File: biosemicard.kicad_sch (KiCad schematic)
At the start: 10 parts, among them J1 Conn_01x12_Pin, J2 Conn_01x08_Pin, U2 74HC151D

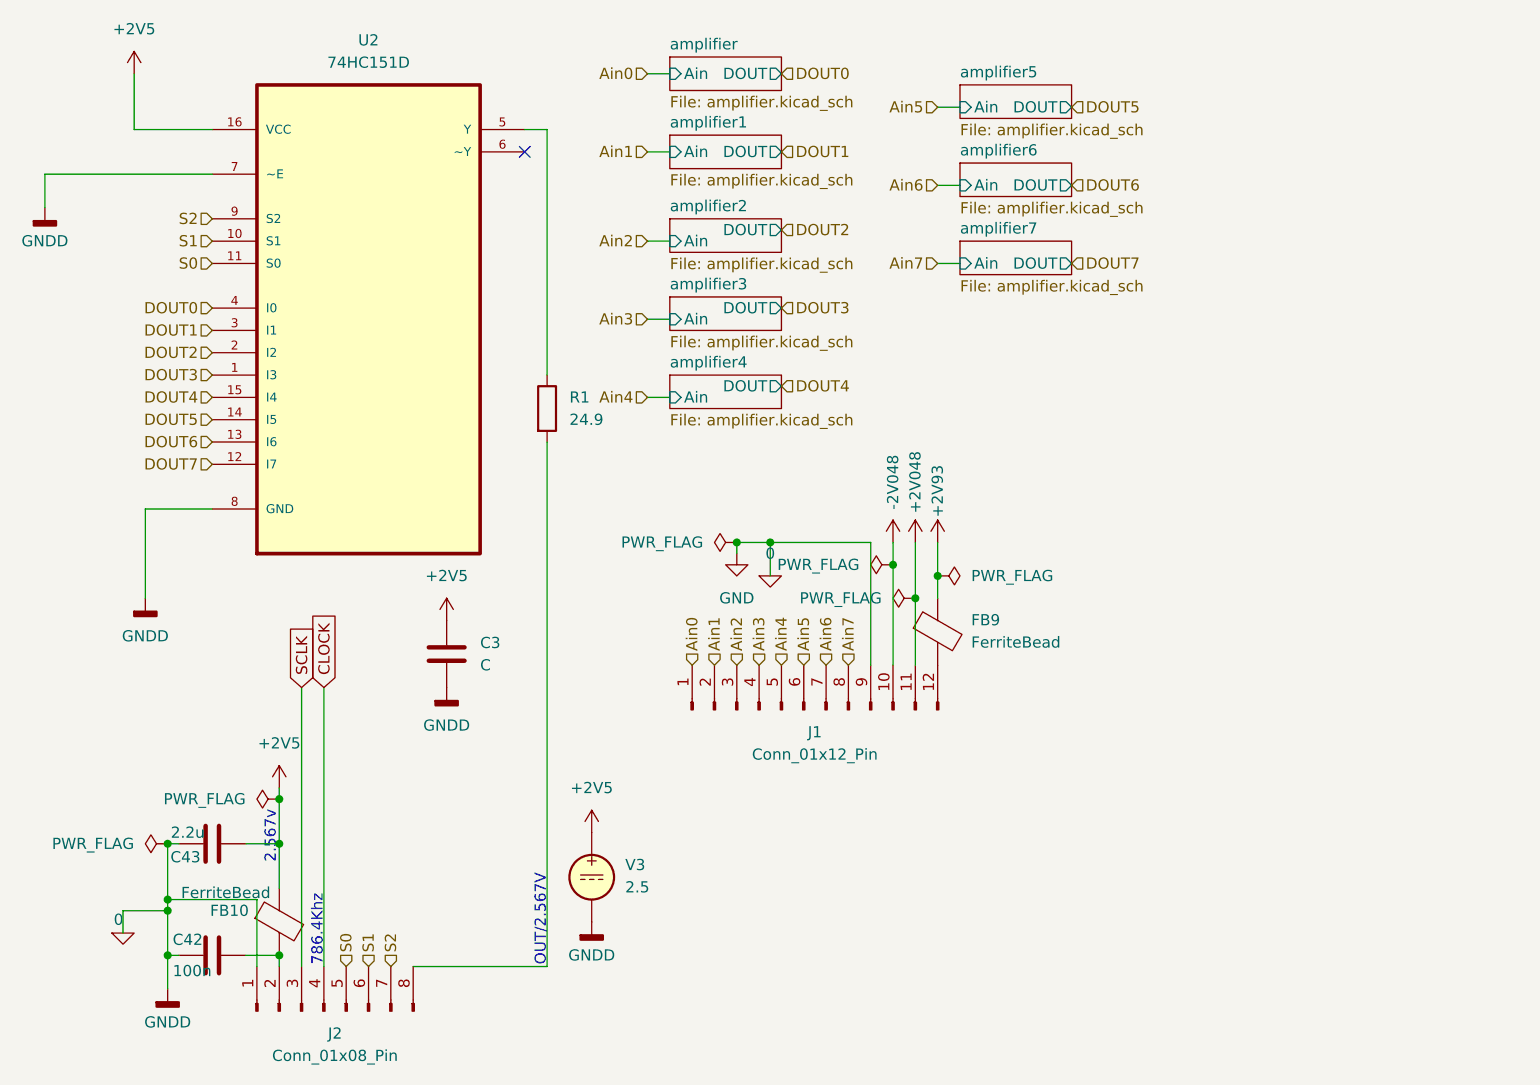
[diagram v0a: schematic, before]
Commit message: added components, updated pcb-routing
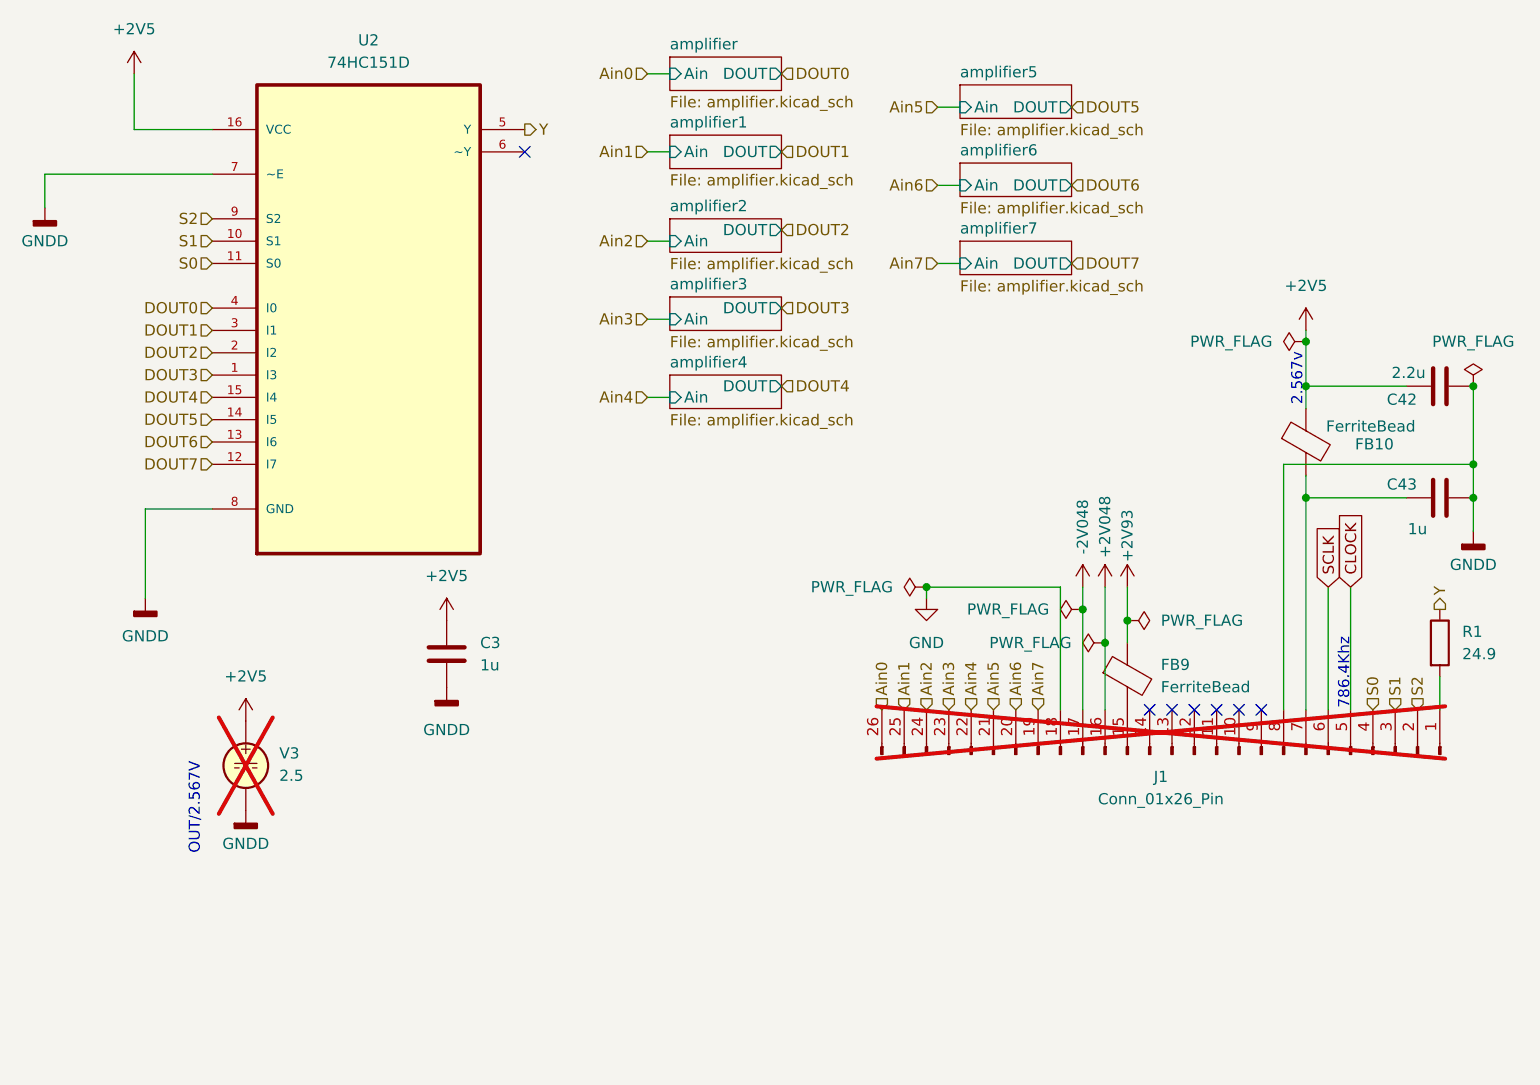
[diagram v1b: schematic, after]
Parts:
- removed J1: Conn_01x12_Pin, symbol Connector:Conn_01x12_Pin
- removed J2: Conn_01x08_Pin, Connector_JST:JST_PH_S7B-PH-K_1x07_P2.00mm_Horizontal, symbol Connector:Conn_01x08_Pin
- added J1: Conn_01x26_Pin, Connector_PinHeader_2.54mm:PinHeader_1x26_P2.54mm_Vertical, symbol Connector:Conn_01x26_Pin
- C3: value C -> 1u; footprint (none) -> Capacitor_SMD:C_0603_1608Metric; LCSC (none) -> C1592
- C42: value 100n -> 2.2u; footprint (none) -> Capacitor_SMD:C_0603_1608Metric; LCSC (none) -> C1607
- C43: value 2.2u -> 1u; footprint (none) -> Capacitor_SMD:C_0603_1608Metric; LCSC (none) -> C1592
- FB10, FB9: LCSC (none) -> C76884
- R1: footprint (none) -> Resistor_SMD:R_0402_1005Metric; LCSC (none) -> C9900186112
- U2: footprint 74HC151D:SOIC127P600X175-16N -> Package_SO:SOIC-16_3.9x9.9mm_P1.27mm; LCSC (none) -> C6822
- V3: now not fitted
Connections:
- net +2V048: now also J1.16 (Pin_16)
- net +2V5: now also C42.1; no longer C43.2
- net -2V048: now also J1.17 (Pin_17)
- net Ain0: now also J1.26 (Pin_26)
- net Ain1: now also J1.25 (Pin_25)
- net Ain2: now also J1.24 (Pin_24)
- net Ain3: now also J1.23 (Pin_23)
- net Ain4: now also J1.22 (Pin_22)
- net Ain5: now also J1.21 (Pin_21)
- net Ain6: now also J1.20 (Pin_20)
- net Ain7: now also J1.19 (Pin_19)
- net CLOCK: now also J1.5 (Pin_5)
- net S0: now also J1.4 (Pin_4)
- net S1: now also J1.3 (Pin_3)
- net S2: now also J1.2 (Pin_2)
- net SCLK: now also J1.6 (Pin_6)
- net Y: now reaches R1.1, U2.5 (Y)
- net at R1.2: now also J1.1 (Pin_1)
- net at FB10.2: now also C43.1, J1.7 (Pin_7); no longer C42.2
- net at FB9.2: now also J1.15 (Pin_15)
- net 0 renamed GNDD
- net GNDD: now also C42.2, C43.2, J1.8 (Pin_8); no longer C42.1, C43.1
- new net GND: J1.18 (Pin_18)
- no-connect marks 1 -> 7
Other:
- moved on the sheet: FB9

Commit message: layout v2
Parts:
- R1: LCSC C9900186112 -> C5099
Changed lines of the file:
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@@
 			)
 		)
-		(property "LCSC" "C9900186112"
+		(property "LCSC" "C5099"
 			(at 175.26 85.09 0)
 			(effects
